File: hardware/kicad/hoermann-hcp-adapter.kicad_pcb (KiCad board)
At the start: 2 copper layers, 100 x 70 mm, 9 parts, among them J1 HCP2 6P6C, U1 ESP32-C3 Super Mini, U2 Isolated RS485

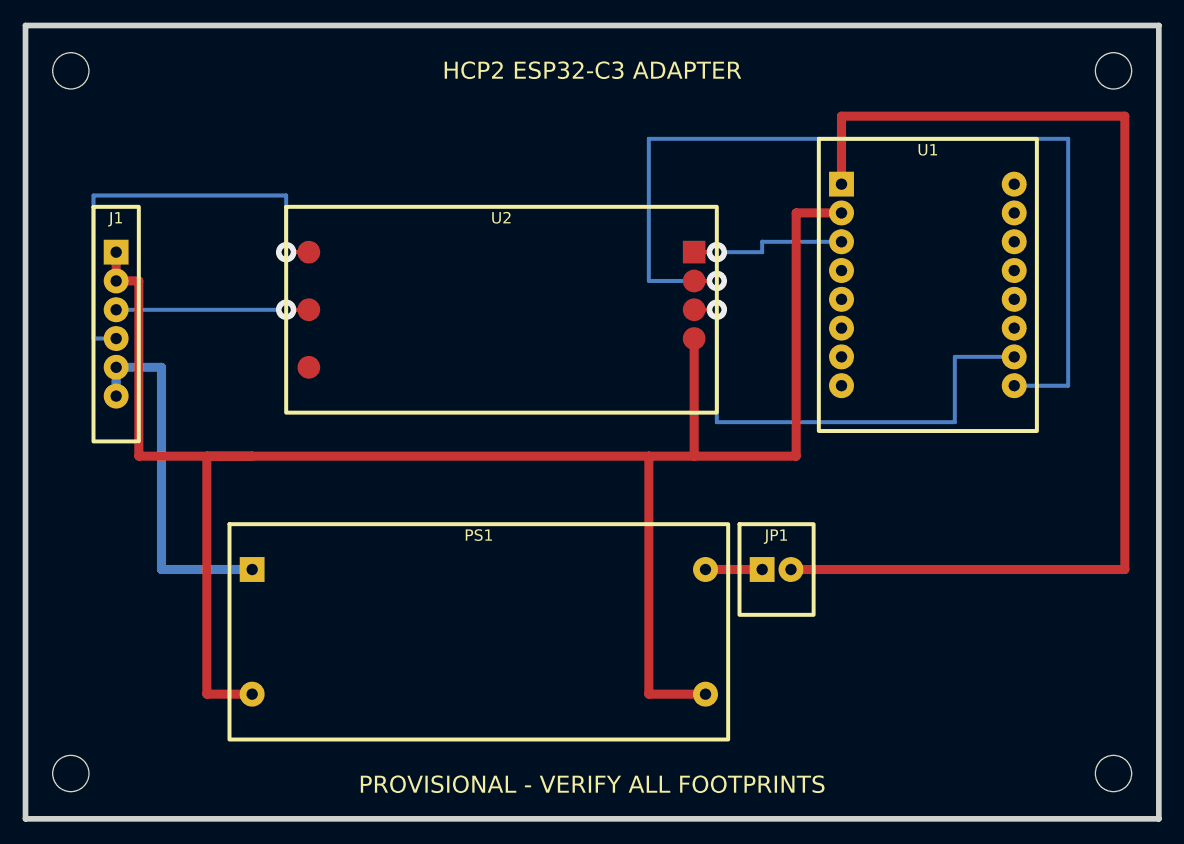
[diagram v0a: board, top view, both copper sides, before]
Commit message: Compact PCB layout with real module footprints
Shrink the board to 63 x 42 mm, put the RJ12 jack at the edge and
replace the placeholder footprints with a project library: KiCad's
Amphenol 54601 footprint for the 95001-type jack, and LM2596 HW-411,
isolated RS485 and ESP32-C3 Super Mini footprints measured from vendor
material. Mounting uses the LM2596 module holes plus one hole under the
ESP32. pcb.py now instantiates library footprints, checks routes against
pad positions and runs DRC; the schematic assigns the same footprints.

Co-Authored-By: Claude Fable 5.1 <noreply@anthropic.com>
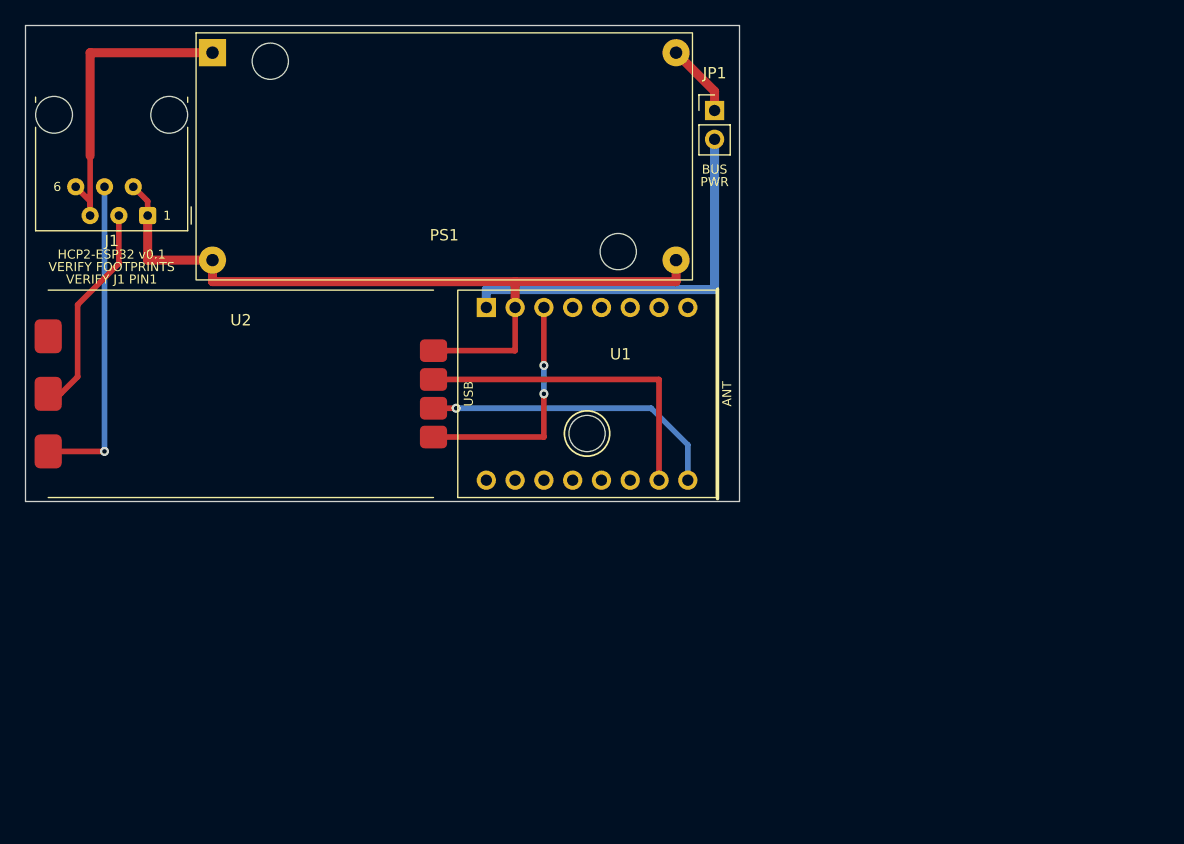
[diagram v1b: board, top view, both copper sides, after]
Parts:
- removed H2: M3, MountingHole:2
- removed H3: M3, MountingHole:3
- removed H4: M3, MountingHole:4
- H1: footprint MountingHole:1 -> HCP:MountingHole_3.2mm_NoCourtyard
- J1: footprint HCP:J1 -> HCP:RJ12_Amphenol_54601-x06_Horizontal
- JP1: footprint HCP:JP1 -> HCP:PinHeader_1x02_P2.54mm_Vertical
- PS1: footprint HCP:PS1 -> HCP:LM2596_HW-411
- U1: footprint HCP:U1 -> HCP:ESP32-C3_SuperMini
- U2: footprint HCP:U2 -> HCP:RS485_Isolated_34x18
- moved H1 55.7 mm to (49.5, 36.0)
- moved JP1 40.7 mm to (60.8, 7.50)
- moved PS1 40.2 mm to (37.0, 11.6)
- moved U1 29.1 mm to (49.5, 32.5), turned to 90 degrees
- moved U2 13.9 mm to (19.0, 32.5), turned to 180 degrees
- moved J1 4.26 mm to (10.8, 16.8), turned to 180 degrees
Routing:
- net HCP_GND: track 168.8 -> 70.7 mm
- net ESP_5V: track 100.5 -> 35.0 mm
- net UART_TX_GPIO21: track 84.1 -> 26.9 mm
- net UART_RX_GPIO20: track 43.9 -> 28.8 mm, vias 1 -> 0
- net HCP_A_PLUS: track 38.6 -> 28.3 mm
- net ESP_3V3: track 13.9 -> 21.2 mm, vias 1 -> 2
- net HCP_25V: track 32.4 -> 28.2 mm
- net HCP_B_MINUS: track 17.0 -> 19.0 mm, vias 1 -> 0
- net BUCK_5V: track 5.00 -> 6.51 mm
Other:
- board size 100 x 70 mm -> 63 x 42 mm
- board text added: "1"
- board text added: "6"
- board text added: "ANT"
- board text added: "BUS"
- board text added: "HCP2-ESP32 v0.1"
- board text added: "PWR"
- board text added: "USB"
- board text added: "VERIFY FOOTPRINTS"
- board text added: "VERIFY J1 PIN1"
- board text removed: "HCP2 ESP32-C3 ADAPTER"
- board text removed: "PROVISIONAL - VERIFY ALL FOOTPRINTS"

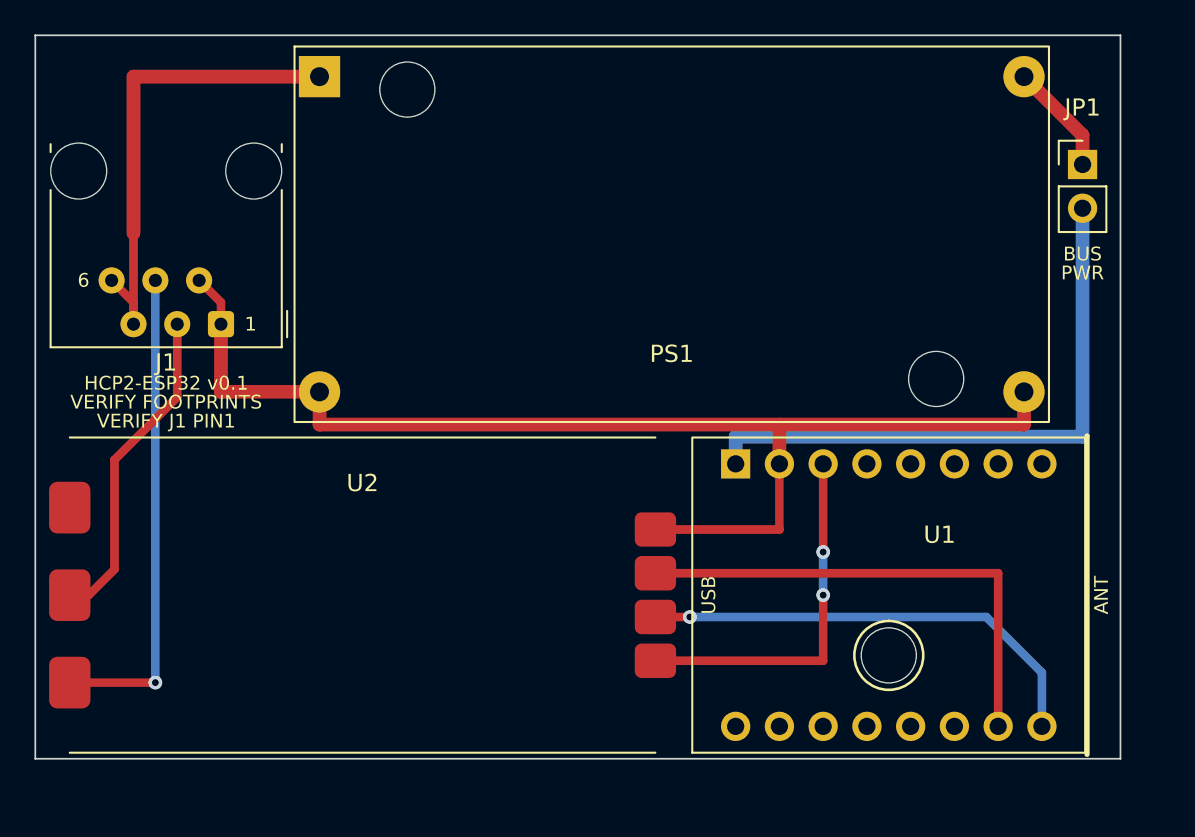
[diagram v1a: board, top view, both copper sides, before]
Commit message: Loosen PCB spacing to 65 x 44.5 mm
About 2 mm between module outlines and 1.5 mm to the board edge.

Co-Authored-By: Claude Fable 5.1 <noreply@anthropic.com>
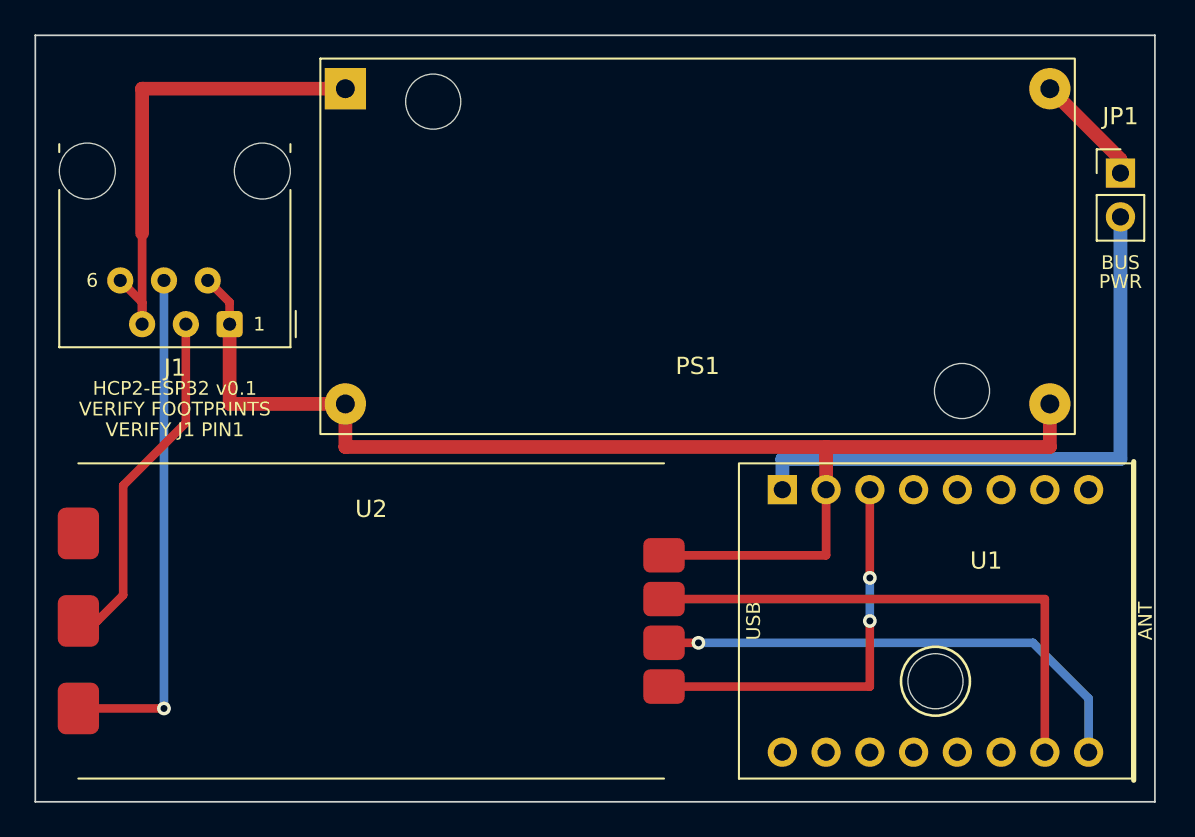
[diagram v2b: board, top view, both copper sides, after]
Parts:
- moved H1 3.10 mm to (52.3, 37.5)
- moved U1 3.10 mm to (52.3, 34.0)
- moved JP1 2.26 mm to (63.0, 8.00)
- moved PS1 1.66 mm to (38.5, 12.2)
- moved U2 1.58 mm to (19.5, 34.0)
- moved J1 0.50 mm to (11.3, 16.8)
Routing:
- net HCP_GND: track 70.7 -> 76.0 mm
- net UART_RX_GPIO20: track 28.8 -> 31.0 mm
- net UART_TX_GPIO21: track 26.9 -> 29.1 mm
- net ESP_3V3: track 21.2 -> 23.4 mm
- net HCP_A_PLUS: track 28.3 -> 29.8 mm
- net HCP_B_MINUS: track 19.0 -> 20.5 mm
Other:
- board size 63 x 42 mm -> 65 x 44.5 mm

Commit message: Add bottom render, layer PDF and silkscreen labels
JP1 gets a "DISCONNECT FOR USB" warning, the back side carries the
project name, version and copyright.

Co-Authored-By: Claude Fable 5.1 <noreply@anthropic.com>
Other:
- board text added: "(C) 2026 Thies Gerken"
- board text added: "DISCONNECT"
- board text added: "FOR USB"
- board text added: "Hörmann HCP2 Adapter v1.0"
- board text added: "Hörmann v1.0"
- board text removed: "HCP2-ESP32 v0.1"
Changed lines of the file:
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@@
   (via (at 7.47 39.08) (size 0.8) (drill 0.4) (layers "F.Cu" "B.Cu") (net 3))
   (gr_rect (start 0 0) (end 65.0 44.5) (stroke (width 0.1) (type default)) (fill none) (layer "Edge.Cuts"))
-  (gr_text "HCP2-ESP32 v0.1" (at 8.1 20.5 0) (layer "F.SilkS") (effects (font (size 0.8 0.8) (thickness 0.15))))
+  (gr_text "Hörmann v1.0" (at 8.1 20.5 0) (layer "F.SilkS") (effects (font (size 0.8 0.8) (thickness 0.15))))
   (gr_text "VERIFY FOOTPRINTS" (at 8.1 21.7 0) (layer "F.SilkS") (effects (font (size 0.8 0.8) (thickness 0.15))))
   (gr_text "VERIFY J1 PIN1" (at 8.1 22.9 0) (layer "F.SilkS") (effects (font (size 0.8 0.8) (thickness 0.15))))
   (gr_text "1" (at 13.0 16.77 0) (layer "F.SilkS") (effects (font (size 0.8 0.8) (thickness 0.15))))
   (gr_text "6" (at 3.3 14.23 0) (layer "F.SilkS") (effects (font (size 0.8 0.8) (thickness 0.15))))
-  (gr_text "BUS" (at 63.0 13.2 0) (layer "F.SilkS") (effects (font (size 0.8 0.8) (thickness 0.15))))
-  (gr_text "PWR" (at 63.0 14.3 0) (layer "F.SilkS") (effects (font (size 0.8 0.8) (thickness 0.15))))
+  (gr_text "BUS" (at 63.0 13.0 0) (layer "F.SilkS") (effects (font (size 0.8 0.8) (thickness 0.15))))
+  (gr_text "PWR" (at 63.0 14.1 0) (layer "F.SilkS") (effects (font (size 0.8 0.8) (thickness 0.15))))
+  (gr_text "DISCONNECT" (at 62.4 19.6 90) (layer "F.SilkS") (effects (font (size 0.8 0.8) (thickness 0.15))))
+  (gr_text "FOR USB" (at 63.6 19.6 90) (layer "F.SilkS") (effects (font (size 0.8 0.8) (thickness 0.15))))
   (gr_text "USB" (at 41.7 34.0 90) (layer "F.SilkS") (effects (font (size 0.8 0.8) (thickness 0.15))))
   (gr_text "ANT" (at 64.45 34.0 90) (layer "F.SilkS") (effects (font (size 0.8 0.8) (thickness 0.15))))
+  (gr_text "Hörmann HCP2 Adapter v1.0" (at 25.0 30.5 0) (layer "B.SilkS") (effects (font (size 1.5 1.5) (thickness 0.15)) (justify mirror)))
+  (gr_text "(C) 2026 Thies Gerken" (at 25.0 33.5 0) (layer "B.SilkS") (effects (font (size 1.2 1.2) (thickness 0.15)) (justify mirror)))
   (embedded_fonts no)
 )
